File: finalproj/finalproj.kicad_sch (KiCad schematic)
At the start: 82 parts, among them J1 Conn_01x01, J10 MotorA Out, J11 MotorB Out, J2 Conn_01x01, J3 Conn_01x01, J4 Programmer_Conn, J5 Stepper_Motor_Controller, J6 Conn_01x01, J7 LIDAR_Connector, J9 RPI_UART_Conn, SW1 SW_DPDT_x2, SW2 SW_DPDT_x2, SW3 SW_Push, U1 LM1085-12, U2 LM1085-12, U3 LM1085-5.0, U4 LM1085-3.3, U5 L298N, U7 STM32F401RCTx, Y1 25 MHz, Y2 32.768 KHz

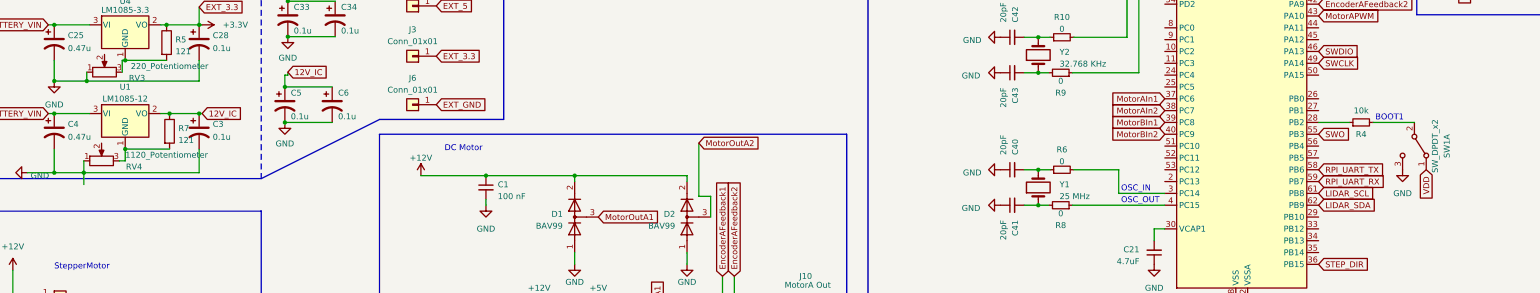
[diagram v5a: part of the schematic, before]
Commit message: added missing footprint libs, changed footprint lib paths to use ${KIPRJMOD}
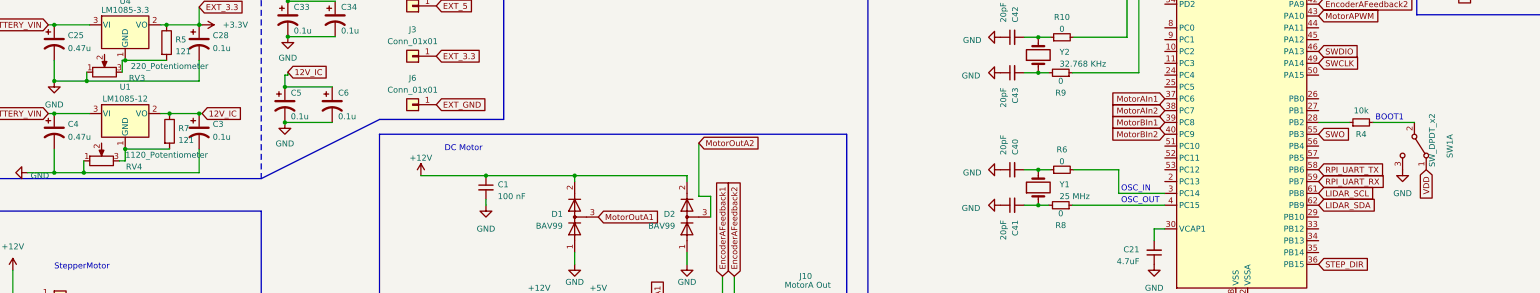
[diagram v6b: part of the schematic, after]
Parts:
- SW1, SW2: footprint EG-1206A:SLIDE-SWITCH -> Switch_E-Switch_EG1206A:SLIDE-SWITCH
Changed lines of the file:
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@@
-    (stroke (width 0) (type default))
-  )
-  (wire (pts (xy 34.29 98.425) (xy 34.29 100.965))
     (stroke (width 0) (type default))
   )
@@
   (symbol (lib_id "Switch:SW_DPDT_x2") (at 320.04 92.71 270) (unit 1)
     (in_bom yes) (on_board yes) (dnp no)
-    (property "Reference" "SW1" (at 327.025 92.71 0)
-      (effects (font (size 1.27 1.27)))
-    )
-    (property "Value" "SW_DPDT_x2" (at 324.485 92.71 0)
-      (effects (font (size 1.27 1.27)))
-    )
-    (property "Footprint" "EG-1206A:SLIDE-SWITCH" (at 320.04 92.71 0)
+    (property "Reference" "SW1" (at 327.66 92.71 0)
+      (effects (font (size 1.27 1.27)))
+    )
+    (property "Value" "SW_DPDT_x2" (at 323.85 91.44 0)
+      (effects (font (size 1.27 1.27)))
+    )
+    (property "Footprint" "Switch_E-Switch_EG1206A:SLIDE-SWITCH" (at 320.04 92.71 0)
       (effects (font (size 1.27 1.27)) hide)
     )
@@
       (effects (font (size 1.27 1.27)))
     )
-    (property "Footprint" "EG-1206A:SLIDE-SWITCH" (at 233.045 49.53 0)
-      (effects (font (size 1.27 1.27)) hide)
-    )
+    (property "Footprint" "Switch_E-Switch_EG1206A:SLIDE-SWITCH" (at 233.045 49.53 0)
+      (effects (font (size 1.27 1.27)) hide)
+    )

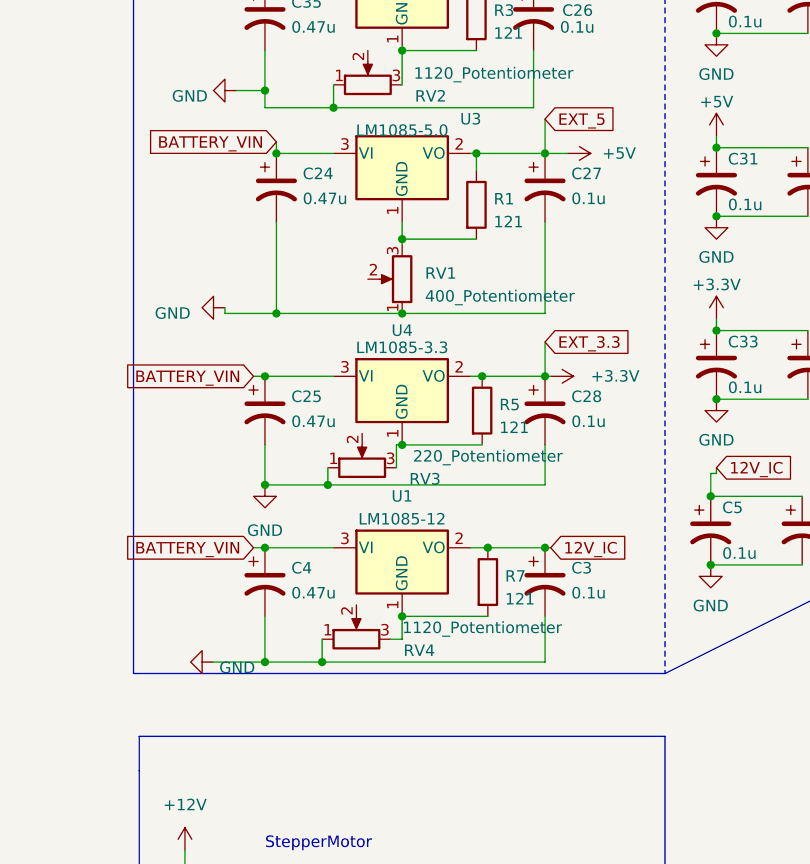
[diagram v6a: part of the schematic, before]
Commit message: fixed switch footprints
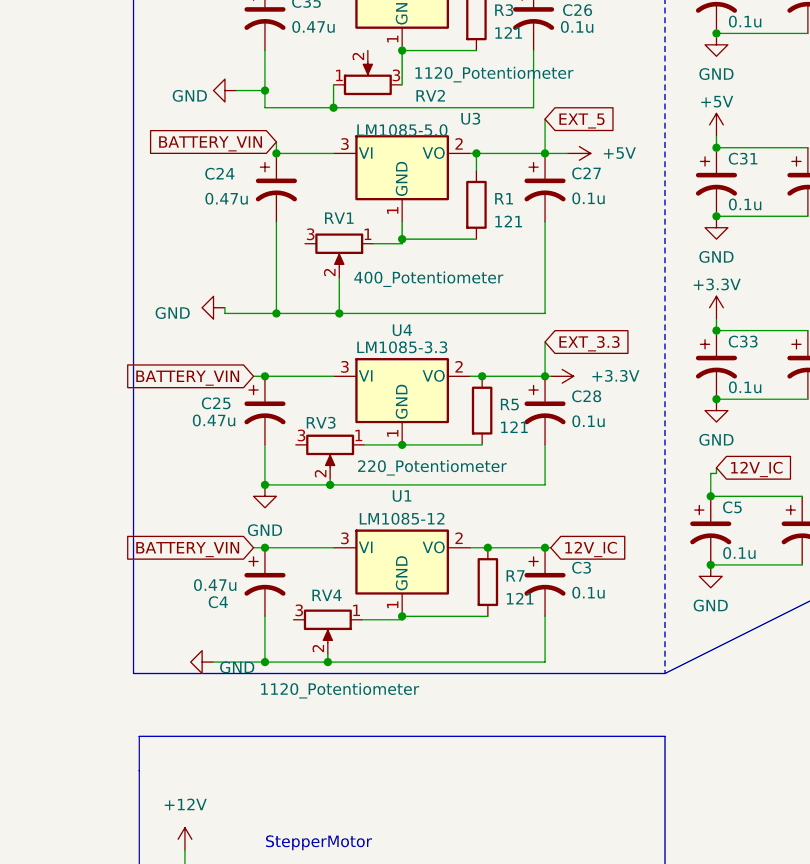
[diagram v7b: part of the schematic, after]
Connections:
- net GND: now also RV1.2, RV3.2, RV4.2; no longer RV1.1, RV3.1, RV4.1
- net at R7.2, U1.1 (GND): now also RV4.1; no longer RV4.3
- net at R1.2, U3.1 (GND): now also RV1.1; no longer RV1.3
- net at R5.2, U4.1 (GND): now also RV3.1; no longer RV3.3
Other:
- moved on the sheet: RV1, RV3, RV4

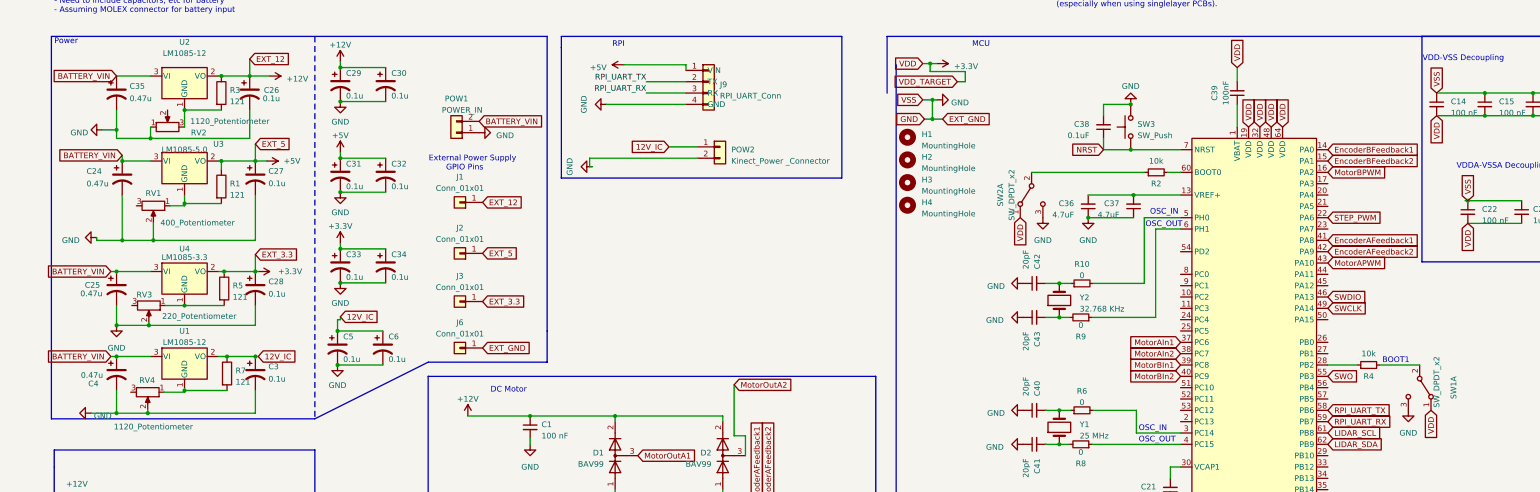
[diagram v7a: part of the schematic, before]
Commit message: made initial placement for each component on PCB, connected MCU passive components
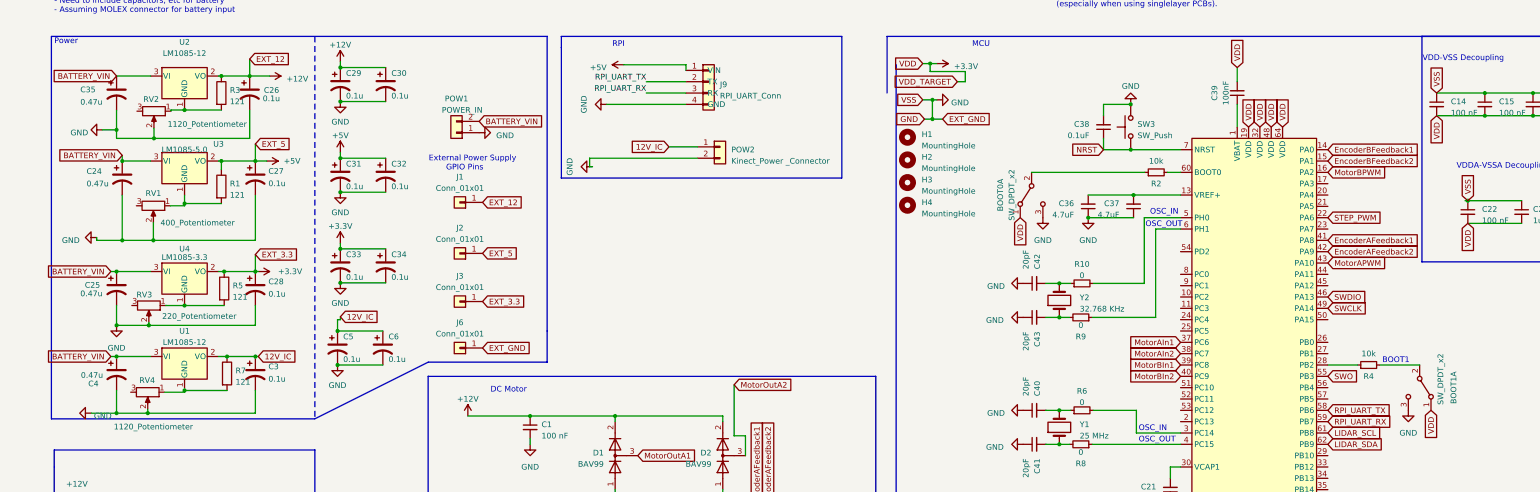
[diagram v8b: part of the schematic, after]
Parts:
- renumbered SW2 to BOOT0, SW1 to BOOT1
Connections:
- net GND: now also RV2.2; no longer RV2.1
- net at R3.2, U2.1 (GND): now also RV2.1; no longer RV2.3
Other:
- moved on the sheet: RV2
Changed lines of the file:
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@@
   (junction (at 356.235 31.75) (diameter 0) (color 0 0 0 0)
   )
-  (junction (at 43.18 30.48) (diameter 0) (color 0 0 0 0)
-  )
-  (junction (at 35.56 36.83) (diameter 0) (color 0 0 0 0)
-  )
   (junction (at 377.825 31.75) (diameter 0) (color 0 0 0 0)
   )
@@
   (junction (at 51.435 41.91) (diameter 0) (color 0 0 0 0)
   )
+  (junction (at 36.322 36.83) (diameter 0) (color 0 0 0 0)
+  )
   (junction (at 245.745 54.61) (diameter 0) (color 0 0 0 0)
   )
+  (junction (at 43.18 30.48) (diameter 0) (color 0 0 0 0)
+  )
   (junction (at 345.44 31.75) (diameter 0) (color 0 0 0 0)
   )
@@
     (stroke (width 0) (type default))
   )
-  (wire (pts (xy 43.18 30.48) (xy 43.18 34.29))
-    (stroke (width 0) (type default))
-  )
   (wire (pts (xy 166.37 103.505) (xy 168.91 103.505))
     (stroke (width 0) (type default))
@@
     (stroke (width 0) (type default))
   )
-  (wire (pts (xy 35.56 34.29) (xy 35.56 36.83))
-    (stroke (width 0) (type default))
-  )
   (wire (pts (xy 167.64 165.1) (xy 176.53 165.1))
     (stroke (width 0) (type default))
@@
     (stroke (width 0) (type default))
   )
+  (wire (pts (xy 36.322 34.544) (xy 36.322 36.83))
+    (stroke (width 0) (type default))
+  )
   (wire (pts (xy 106.68 99.06) (xy 120.65 99.06))
     (stroke (width 0) (type default))
@@
     (stroke (width 0) (type default))
   )
+  (wire (pts (xy 40.132 30.734) (xy 40.132 30.48))
+    (stroke (width 0) (type default))
+  )
   (wire (pts (xy 22.86 165.1) (xy 22.86 147.32))
     (stroke (width 0) (type default))
@@
     (stroke (width 0) (type default))
   )
+  (wire (pts (xy 43.18 30.48) (xy 51.435 30.48))
+    (stroke (width 0) (type default))
+  )
   (wire (pts (xy 59.055 74.295) (xy 59.055 78.74))
     (stroke (width 0) (type default))
@@
     (stroke (width 0) (type default))
   )
-  (wire (pts (xy 27.94 36.83) (xy 35.56 36.83))
+  (wire (pts (xy 27.94 36.83) (xy 36.322 36.83))
     (stroke (width 0) (type default))
   )
@@
     (stroke (width 0) (type default))
   )
+  (wire (pts (xy 36.322 36.83) (xy 57.785 36.83))
+    (stroke (width 0) (type default))
+  )
   (wire (pts (xy 137.16 127) (xy 137.16 129.54))
     (stroke (width 0) (type default))
@@
     (stroke (width 0) (type default))
   )
-  (wire (pts (xy 43.18 30.48) (xy 51.435 30.48))
+  (wire (pts (xy 40.132 30.48) (xy 43.18 30.48))
     (stroke (width 0) (type default))
   )
@@
     (stroke (width 0) (type default))
   )
-  (wire (pts (xy 35.56 36.83) (xy 57.785 36.83))
-    (stroke (width 0) (type default))
-  )
   (wire (pts (xy 22.225 98.425) (xy 27.94 98.425))
     (stroke (width 0) (type default))
@@
     )
   )
-  (symbol (lib_id "Device:R_Potentiometer") (at 39.37 34.29 90) (unit 1)
+  (symbol (lib_id "Device:R_Potentiometer") (at 36.322 30.734 270) (unit 1)
     (in_bom yes) (on_board yes) (dnp no)
-    (property "Reference" "RV2" (at 46.355 35.56 90)
+    (property "Reference" "RV2" (at 35.687 28.067 90)
       (effects (font (size 1.27 1.27)))
     )
-    (property "Value" "1120_Potentiometer" (at 53.34 33.02 90)
+    (property "Value" "1120_Potentiometer" (at 48.26 33.655 90)
       (effects (font (size 1.27 1.27)))
     )
-    (property "Footprint" "Potentiometer_SMD:Potentiometer_Bourns_TC33X_Vertical" (at 39.37 34.29 0)
+    (property "Footprint" "Potentiometer_SMD:Potentiometer_Bourns_TC33X_Vertical" (at 36.322 30.734 0)
       (effects (font (size 1.27 1.27)) hide)
     )
-    (property "Datasheet" "~" (at 39.37 34.29 0)
+    (property "Datasheet" "~" (at 36.322 30.734 0)
       (effects (font (size 1.27 1.27)) hide)
     )
@@
   (symbol (lib_id "Switch:SW_DPDT_x2") (at 320.04 92.71 270) (unit 1)
     (in_bom yes) (on_board yes) (dnp no)
-    (property "Reference" "SW1" (at 327.66 92.71 0)
+    (property "Reference" "BOOT1" (at 327.66 92.71 0)
       (effects (font (size 1.27 1.27)))
     )
-    (property "Value" "SW_DPDT_x2" (at 323.85 91.44 0)
+    (property "Value" "SW_DPDT_x2" (at 324.739 90.805 0)
       (effects (font (size 1.27 1.27)))
     )
@@
       (project "finalproj"
         (path "/08d1c057-d836-4496-aa4e-f556547e7c14"
-          (reference "SW1") (unit 1)
+          (reference "BOOT1") (unit 1)
         )
       )
@@
   (symbol (lib_id "Switch:SW_DPDT_x2") (at 233.045 49.53 90) (mirror x) (unit 1)
     (in_bom yes) (on_board yes) (dnp no)
-    (property "Reference" "SW2" (at 226.06 49.53 0)
+    (property "Reference" "BOOT0" (at 226.06 49.53 0)
       (effects (font (size 1.27 1.27)))
     )
@@
       (project "finalproj"
         (path "/08d1c057-d836-4496-aa4e-f556547e7c14"
-          (reference "SW2") (unit 1)
+          (reference "BOOT0") (unit 1)
         )
       )
@@
   )
   (symbol (lib_id "Device:C_Polarized_US") (at 27.94 26.67 0) (unit 1)
-    (in_bom yes) (on_board yes) (dnp no) (fields_autoplaced)
-    (property "Reference" "C35" (at 30.861 25.1265 0)
+    (in_bom yes) (on_board yes) (dnp no)
+    (property "Reference" "C35" (at 19.812 25.908 0)
       (effects (font (size 1.27 1.27)) (justify left))
     )
-    (property "Value" "0.47u" (at 30.861 27.9016 0)
+    (property "Value" "0.47u" (at 19.812 28.6831 0)
       (effects (font (size 1.27 1.27)) (justify left))
     )
